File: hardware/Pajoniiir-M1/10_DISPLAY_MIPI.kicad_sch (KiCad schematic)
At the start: 30 parts

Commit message: hardware: fix local symbol cache keys for ERC
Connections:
- net 5V_SYS: now also U_BL.3 (FB), U_BL.4 (EN)
- net BL_EN: now also U_BL.6 (IN)
- net LEDA: now also U_BL.5 (OV)
- net LEDK: now also U_BL.1 (SW)

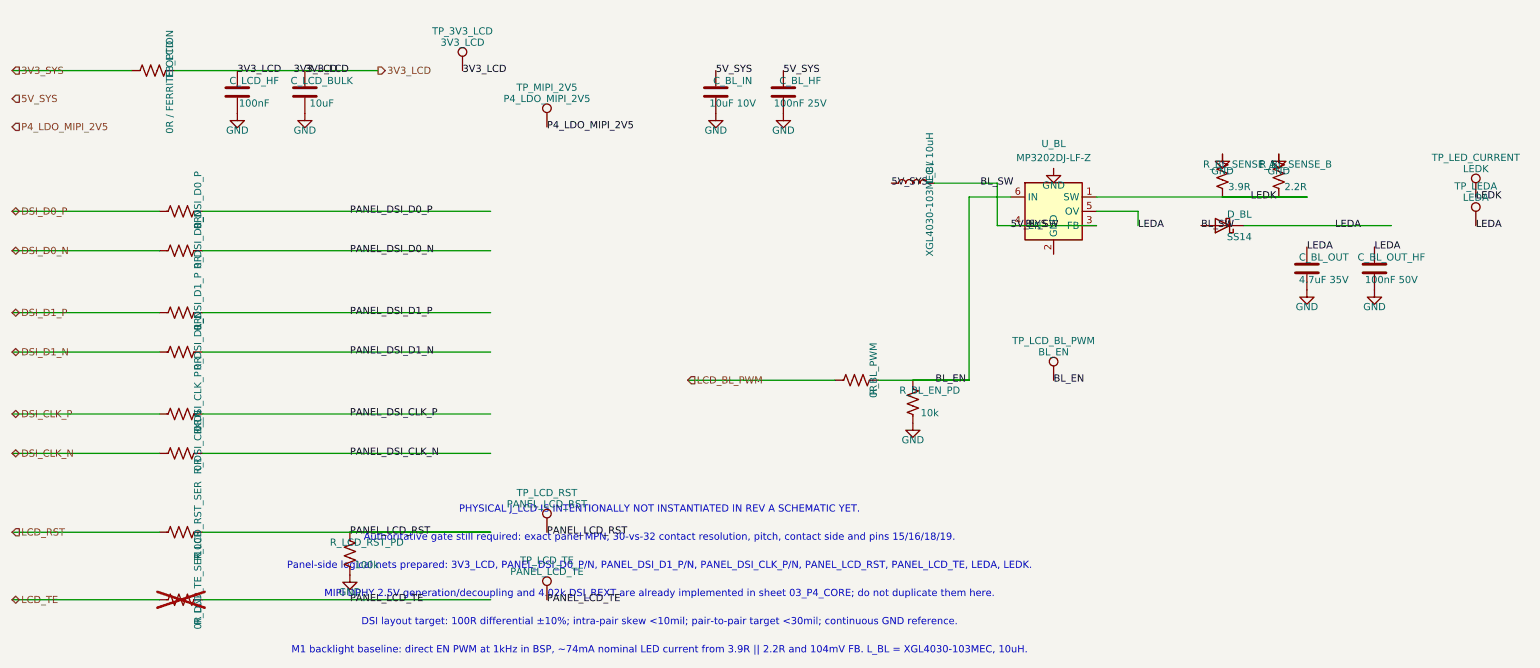
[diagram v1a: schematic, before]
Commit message: hardware: snap child sheets 06-10 to 25 mil grid
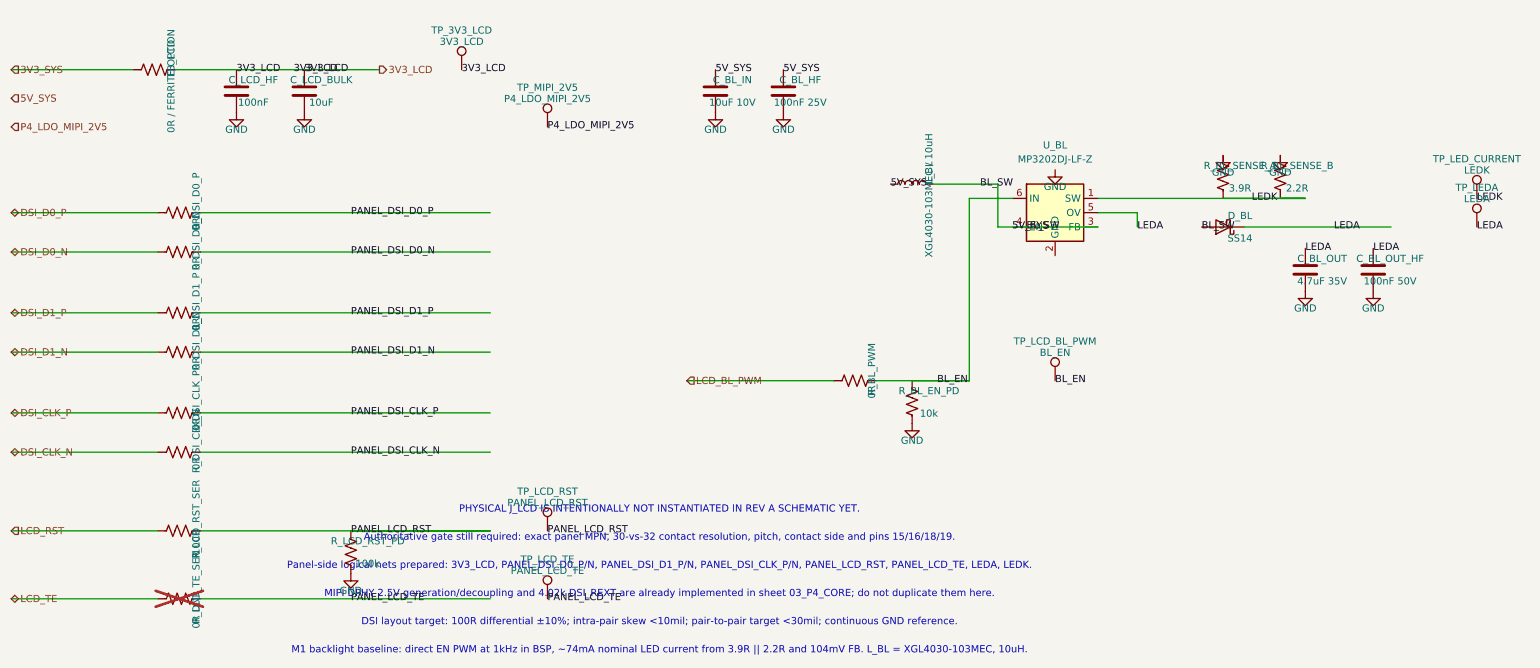
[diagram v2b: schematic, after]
